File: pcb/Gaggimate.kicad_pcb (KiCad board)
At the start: 2 copper layers, 85 x 67 mm, 108 parts, among them J1 USB_C_Receptacle, J10 Conn_01x02, J2 Conn_01x02, J3 Conn_01x03, J4 Conn_01x04, J5 Conn_01x04, J6 Conn_01x10, J7 Conn_01x02, J8 Conn_01x02, J9 Conn_01x04, K1 Relay_SPDT, K2 Relay_SPDT, K3 Relay_SPDT, Q1 MMBT2222A, Q2 MMBT2222A, Q3 MMBT2222A, SW1 SW_Push, SW2 SW_Push, U1 ESP32-S3-WROOM-1, U2 AMS1117-3.3, U3 USBLC6-2SC6, U6 MAX31855EASA

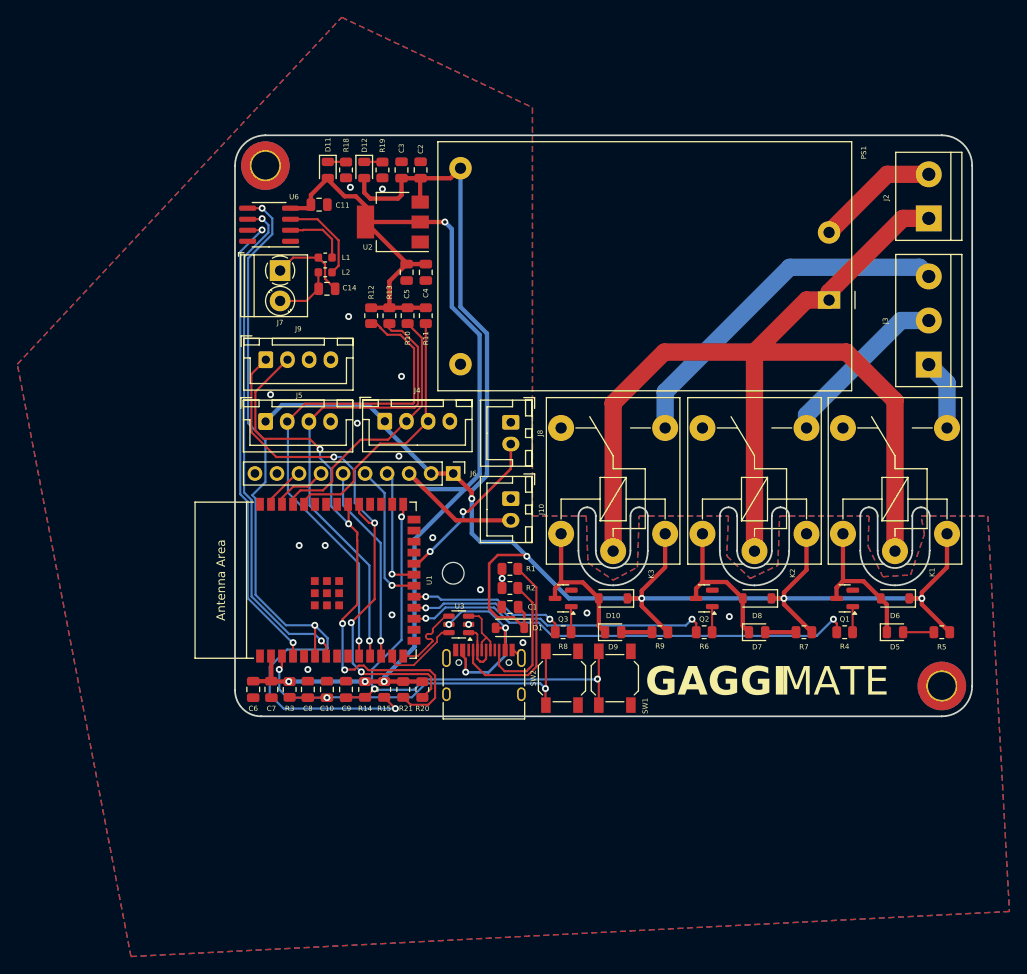
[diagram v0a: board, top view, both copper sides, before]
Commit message: feat: Add adjustments to PCB, pcb diff pipeline
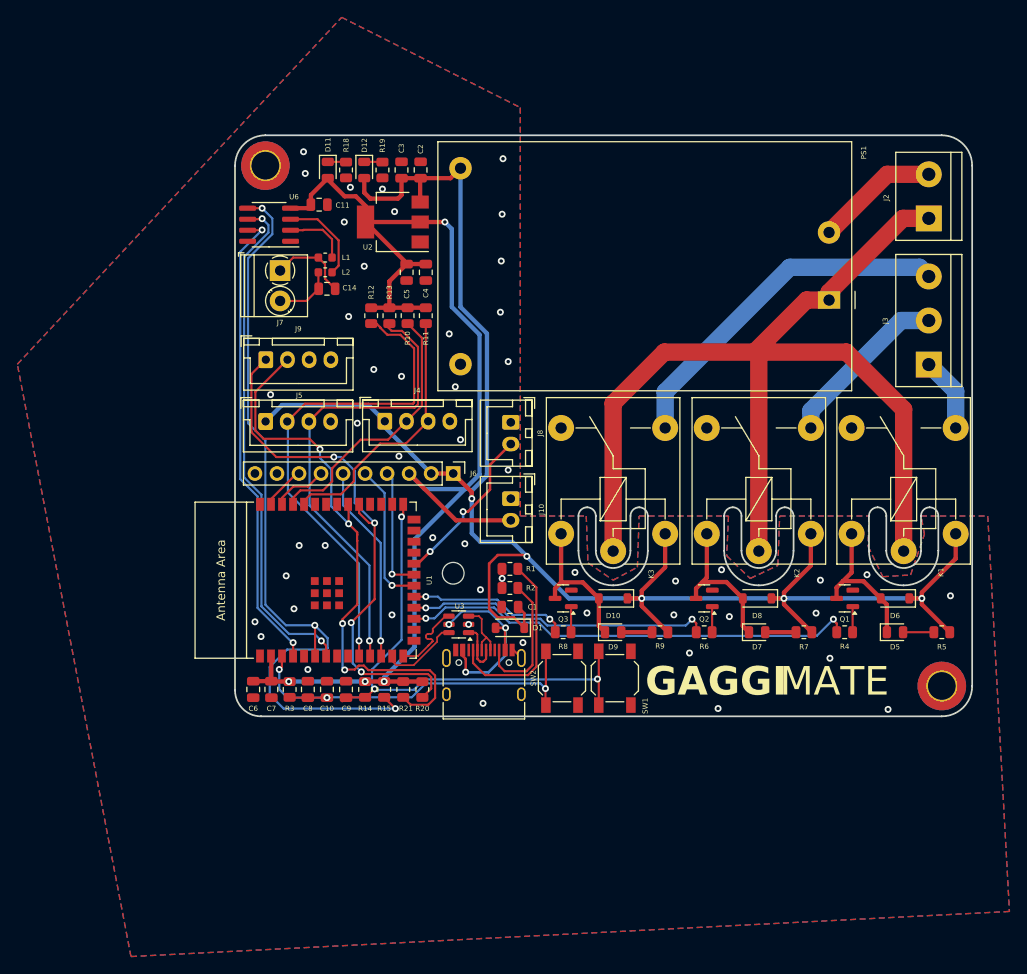
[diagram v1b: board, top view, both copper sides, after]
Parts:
- moved K1 1.00 mm to (238.8, 74.0)
- moved K2 0.50 mm to (222.1, 74.0)
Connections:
- D6 pad 1: unconnected-(D6-K-Pad1) -> +5V
- K1 pad A1: Net-(K1-PadA1) -> +5V
- R5 pad 2: Net-(K1-PadA1) -> +5V
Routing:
- net /SPI_CLK: track 92.7 -> 91.5 mm
- net LINE: track 121.6 -> 122.2 mm
- net Net-(D5-K): track 17.1 -> 16.5 mm
- net GND: vias 18 -> 51
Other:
- outline, holes or cut-outs redrawn
